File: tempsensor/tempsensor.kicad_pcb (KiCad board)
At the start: 2 copper layers, 40 x 40 mm, 68 parts, among them J1 USB_B_Micro, Q1 BC817, Q2 BC817, Q3 BC817, Q4 BSS806N, SW1 PW_OFF, SW2 PW_OFF, SW3 PW_ON, U2 ESP-12F, U3 24C16, U4 MCP73831-2-OT, U5 MCP9844, U6 MAX17620

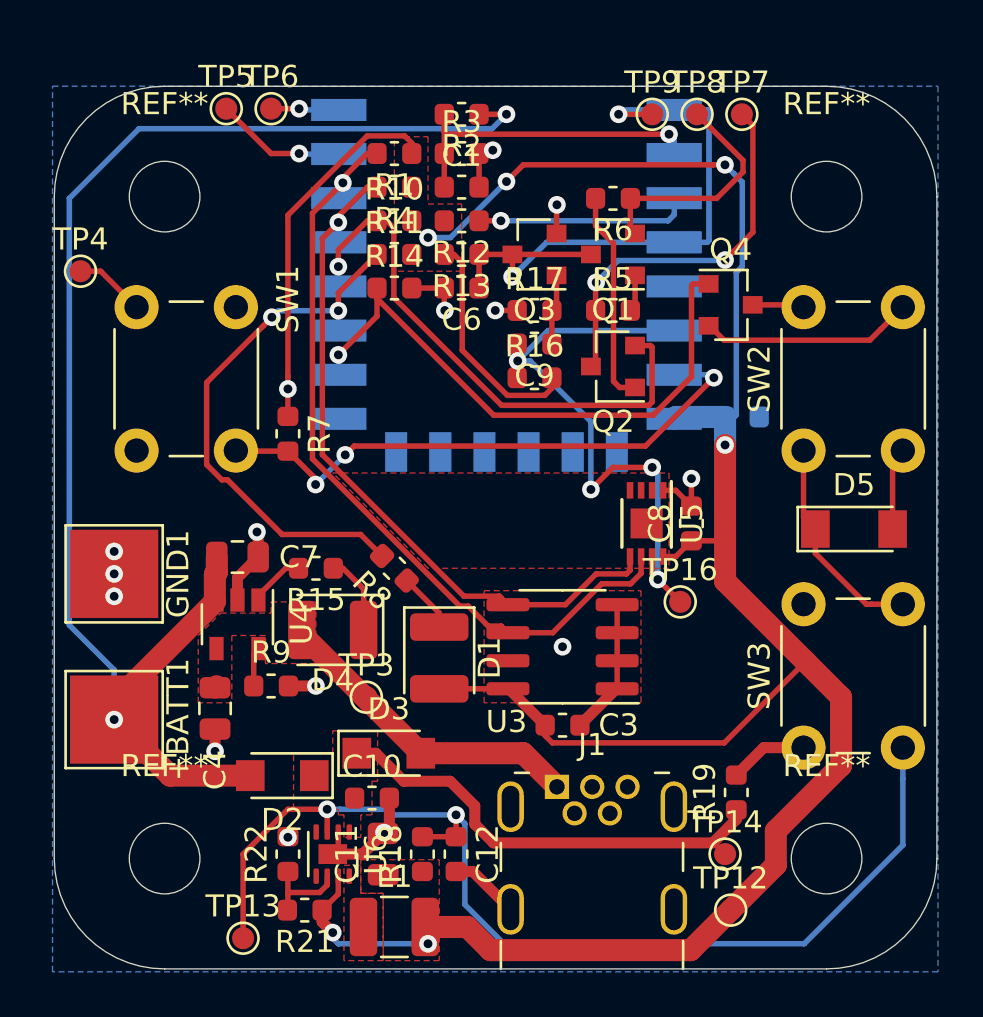
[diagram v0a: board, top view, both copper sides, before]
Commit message: Finished layouting, exchanged two false diode packages, added protection diode to RTC reset line output, updated config button circuit.
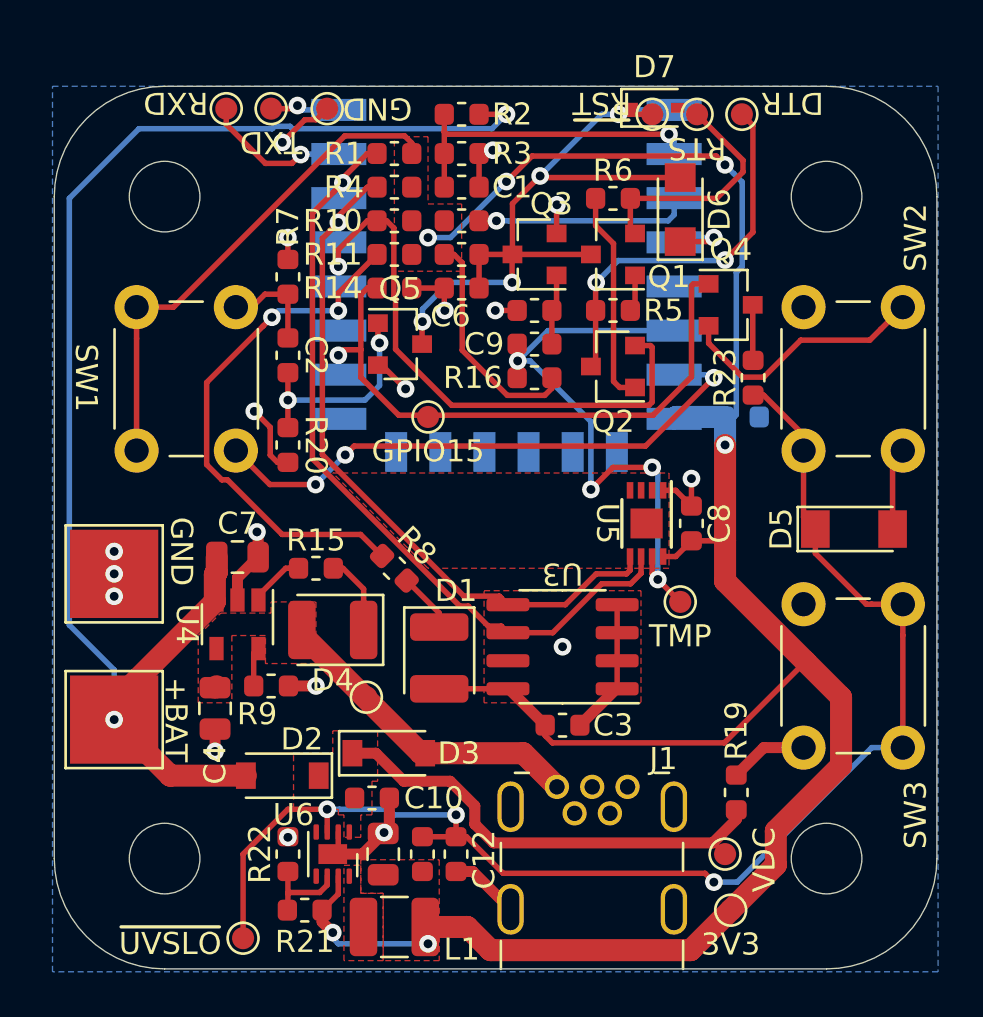
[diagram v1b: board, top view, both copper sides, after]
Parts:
- added C2: 1u, Capacitor_SMD:C_0603_1608Metric, F.Cu at (188.5, 80.8)
- added D6: SL03, Diode_SMD:D_SMF, F.Cu at (206.2, 74.2)
- added D7: NSR0340HT1G, Diode_SMD:D_SOD-323, F.Cu at (205.1, 69.6)
- added Q5: BC817, Package_TO_SOT_SMD:SOT-23, F.Cu at (193.5, 80.3)
- added R20: 4K7, Resistor_SMD:R_0603_1608Metric, F.Cu at (188.5, 84.8)
- added R23: 0R37, Resistor_SMD:R_0603_1608Metric, F.Cu at (209.6, 81.8)
- added TP1: GPIO15, TestPoint:TestPoint_Pad_D1.0mm, F.Cu at (194.8, 83.6)
- D2, D3: footprint Diode_SMD:D_SMF -> Diode_SMD:D_SOD-123
- R7: value 10K -> 4K7
- moved TP4 13.4 mm to (190.2, 69.6)
- moved R7 7.11 mm to (188.5, 77.2)
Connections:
- Q4 pad 3: /~UVSLO -> Net-(Q4-Pad3)
- R7 pad 1: +3V3 -> GND
- SW1 pad 1: GND -> +3V3
- U2 pad 4: /~RST -> Net-(D6-Pad1)
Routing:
- net Net-(C2-Pad1): track 0.00 -> 9.77 mm, vias 0 -> 2
- net GND: track 47.1 -> 54.3 mm, vias 14 -> 18
- net +3V3: track 128.7 -> 135.0 mm, vias 7 -> 6
- net /~RST: track 28.8 -> 33.3 mm, vias 2 -> 4
- net /CONF: track 26.3 -> 30.8 mm
- net Net-(D6-Pad1): track 0.00 -> 3.49 mm, vias 0 -> 1
- net Net-(Q4-Pad3): track 0.00 -> 2.52 mm
- net /GPIO0: track 25.1 -> 26.4 mm
- net /RXD: track 5.95 -> 6.72 mm
- net /GPIO15: track 27.2 -> 28.0 mm
- net /~UVSLO: track 61.2 -> 61.8 mm, vias 2 -> 3

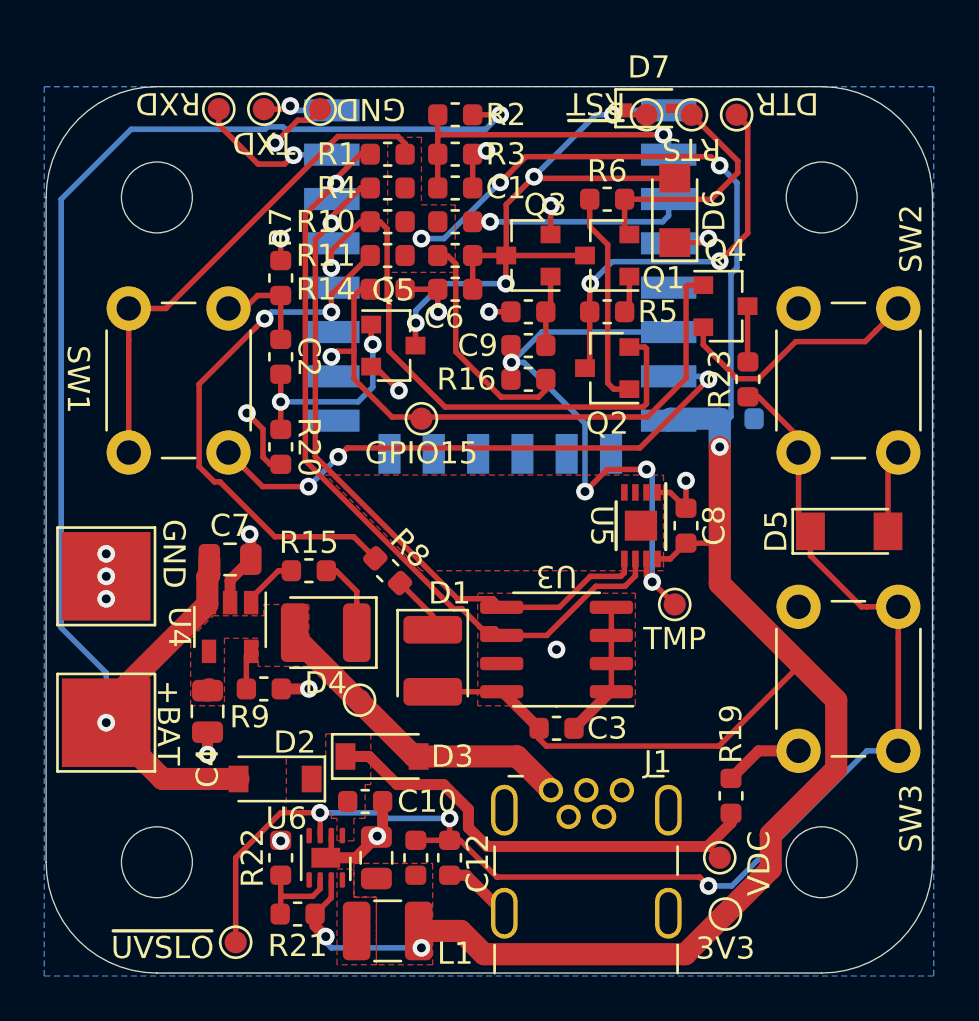
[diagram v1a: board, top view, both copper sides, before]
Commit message: Created base schematic for MKW41 tempsensor, still need to finetune it.
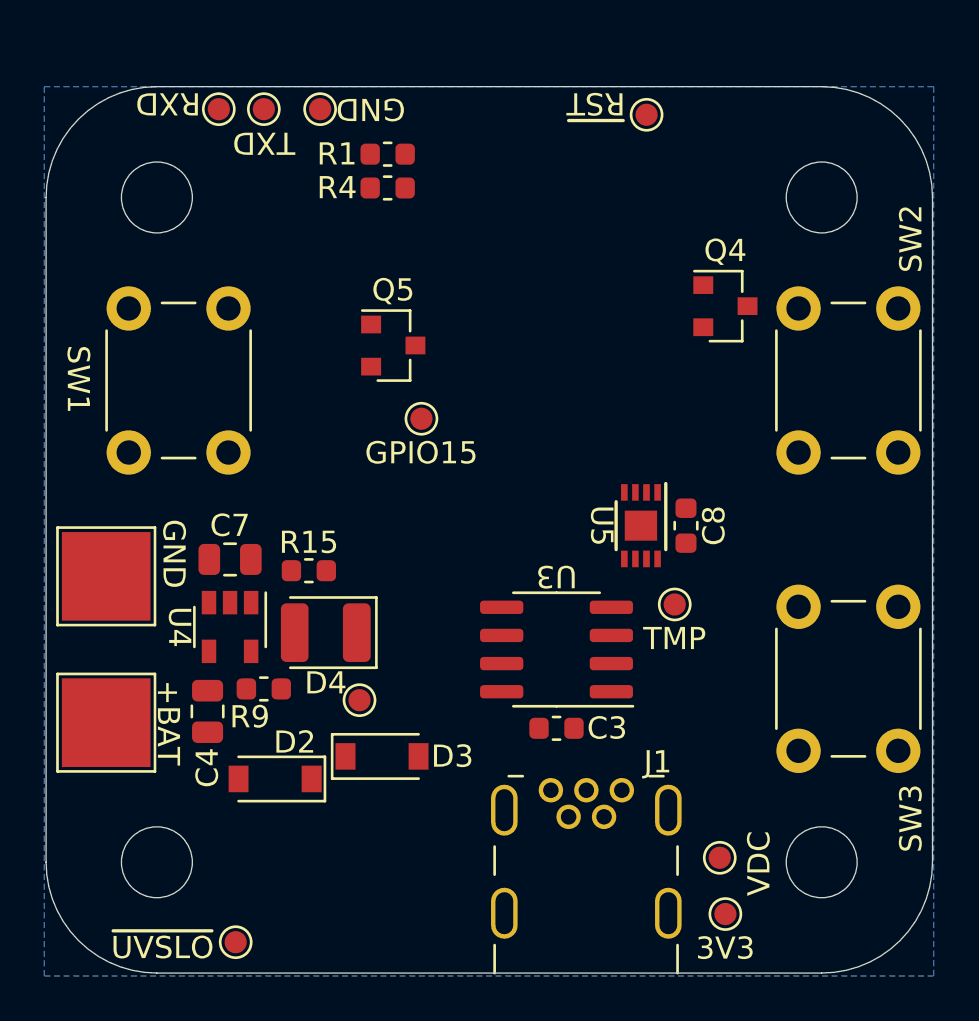
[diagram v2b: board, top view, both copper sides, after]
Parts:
- removed C1: 10n, Capacitor_SMD:C_0603_1608Metric
- removed C10: 2u2, Capacitor_SMD:C_0603_1608Metric
- removed C11: 10u, Capacitor_SMD:C_0805_2012Metric
- removed C12, C2, C5, C9: 1u, Capacitor_SMD:C_0603_1608Metric
- removed C6: 100n, Capacitor_SMD:C_0603_1608Metric
- removed D1: LED, LED_SMD:LED_1210_3225Metric
- removed D5: ZMM3V3, Diode_SMD:D_MiniMELF
- removed D6: SL03, Diode_SMD:D_SMF
- removed D7: NSR0340HT1G, Diode_SMD:D_SOD-323
- removed L1: 1u, Inductor_SMD:L_1210_3225Metric
- removed Q1, Q2, Q3: BC817, Package_TO_SOT_SMD:SOT-23
- removed R10, R11, R12, R13, R14, R18, R19, R5, R6: 10K, Resistor_SMD:R_0603_1608Metric
- removed R16, R22, R3: 100K, Resistor_SMD:R_0603_1608Metric
- removed R17, R20, R7: 4K7, Resistor_SMD:R_0603_1608Metric
- removed R2: 430K, Resistor_SMD:R_0603_1608Metric
- removed R21: 313K, Resistor_SMD:R_0603_1608Metric
- removed R23: 0R37, Resistor_SMD:R_0603_1608Metric
- removed R8: 330, Resistor_SMD:R_0603_1608Metric
- removed TP7: DTR, TestPoint:TestPoint_Pad_D1.0mm
- removed TP8: RTS, TestPoint:TestPoint_Pad_D1.0mm
- removed U2: ESP-12F, RF_Module:ESP-12E
- removed U6: MAX17620, Package_DFN_QFN:DFN-8-1EP_2x2mm_P0.5mm_EP0.9x1.3mm
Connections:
- J1 pad 2: Net-(J1-Pad2) -> (no net)
- J1 pad 3: Net-(J1-Pad3) -> (no net)
- J1 pad 4: Net-(J1-Pad4) -> (no net)
- Q4 pad 1: /GPIO15 -> (no net)
- Q4 pad 2: GND -> (no net)
- Q4 pad 3: Net-(Q4-Pad3) -> (no net)
- Q5 pad 1: Net-(C2-Pad1) -> (no net)
- Q5 pad 2: GND -> (no net)
- Q5 pad 3: /~RST -> (no net)
- SW1 pad 1: +3V3 -> Net-(SW1-Pad1)
- SW1 pad 2: /CONF -> Net-(SW1-Pad2)
- SW2 pad 1: /~UVSLO -> Net-(SW2-Pad1)
- SW2 pad 2: GND -> Net-(SW2-Pad2)
- SW3 pad 2: /~UVSLO -> Net-(SW3-Pad2)
- TP1 pad 1: /GPIO15 -> (no net)
- TP13 pad 1: /~UVSLO -> (no net)
- TP16 pad 1: /TMP -> (no net)
- TP5 pad 1: /RXD -> (no net)
- TP6 pad 1: /TXD -> (no net)
- TP9 pad 1: /~RST -> (no net)
- U5 pad 7: /TMP -> (no net)
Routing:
- net +3V3: track 135.0 -> 0.00 mm, vias 6 -> 0
- net +BATT: track 63.5 -> 0.00 mm, vias 2 -> 0
- net /~UVSLO: track 61.8 -> 0.00 mm, vias 3 -> 0
- net GND: track 54.3 -> 0.00 mm, vias 18 -> 0
- net /SCL: track 36.5 -> 0.00 mm, vias 1 -> 0
- net /~RST: track 33.3 -> 0.00 mm, vias 4 -> 0
- net /SDA: track 32.3 -> 0.00 mm, vias 1 -> 0
- net /CONF: track 30.8 -> 0.00 mm, vias 3 -> 0
- net /GPIO15: track 28.0 -> 0.00 mm, vias 1 -> 0
- net /TMP: track 27.7 -> 0.00 mm, vias 4 -> 0
- net /GPIO0: track 26.4 -> 0.00 mm, vias 1 -> 0
- net /GPIO2: track 24.9 -> 0.00 mm, vias 2 -> 0
- net +VDC: track 21.0 -> 0.00 mm
- net /DTR: track 17.5 -> 0.00 mm, vias 2 -> 0
- net VBUS: track 15.0 -> 0.00 mm
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- removed copper zone on F.Cu, net +3V3
- removed copper zone on F.Cu, net +VDC
- removed copper zone on F.Cu, net GND
- removed copper zone on F.Cu, net Net-(L1-Pad1)
- removed copper zone on F.Cu, net VBUS
